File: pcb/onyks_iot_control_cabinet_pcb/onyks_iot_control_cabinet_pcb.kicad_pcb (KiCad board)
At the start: 2 copper layers, 80 x 90 mm, 37 parts, among them J1 Conn_01x02_Socket, J10 Conn_02x05_Odd_Even, J2 Conn_01x06_Socket, J3 Screw_Terminal_01x02, J4 Jack-DC, J6 Conn_02x09_Odd_Even, J7 Screw_Terminal_01x02, J8 Conn_01x06_Pin, J9 Conn_01x02_Socket, Q1 SQ4050EY-T1_GE3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

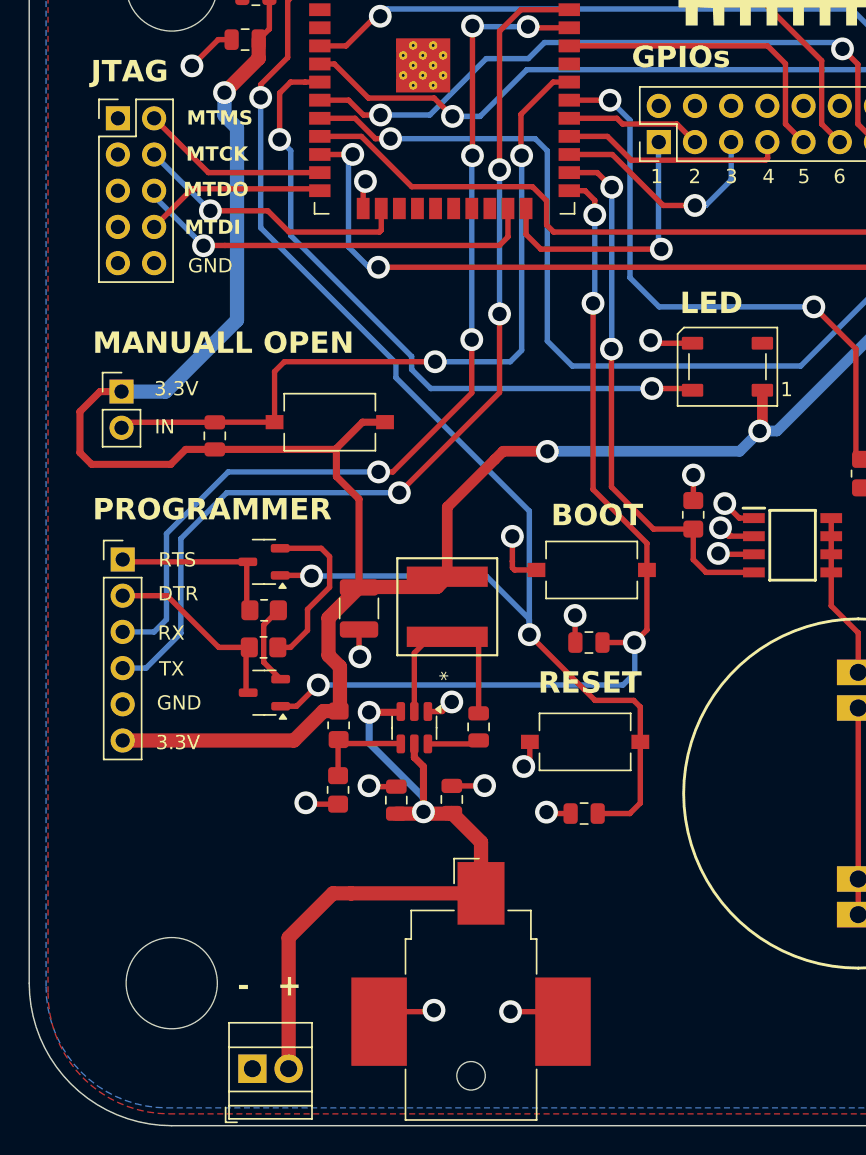
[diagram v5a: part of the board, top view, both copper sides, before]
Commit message: Add pins for the jumper and choosing the power supply; also add connection for JTAG 3V3
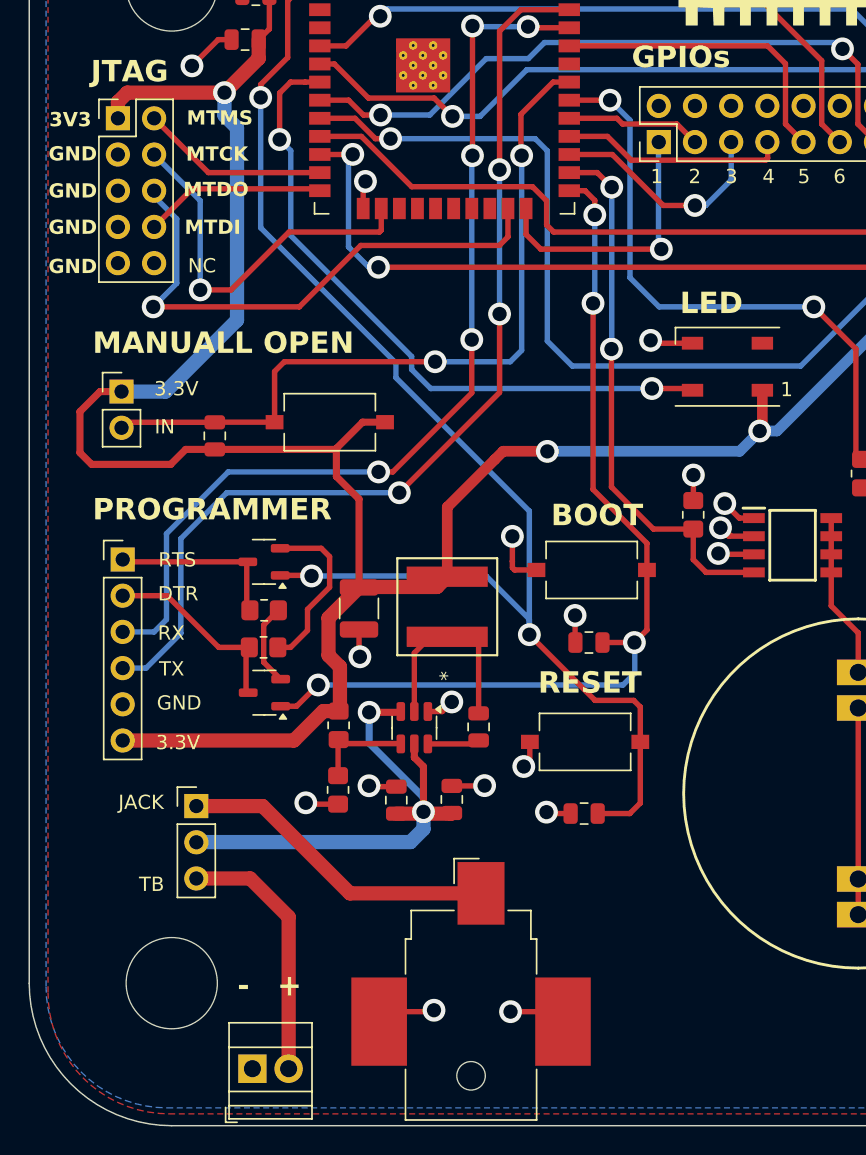
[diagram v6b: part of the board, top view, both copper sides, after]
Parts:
- added J5: Conn_01x03_Pin, Connector_PinHeader_2.54mm:PinHeader_1x03_P2.54mm_Vertical, F.Cu at (57.7, 93.6)
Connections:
- J10 pad 1: unconnected-(J10-Pin_1-Pad1) -> +3.3V
- J3 pad 2: V_IN -> Net-(J3-Pin_2)
- J4 pad 1: V_IN -> Net-(J5-Pin_1)
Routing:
- net Net-(J5-Pin_1): track 0.00 -> 22.5 mm
- net Net-(J3-Pin_2): track 0.00 -> 18.2 mm
- net V_IN: track 50.4 -> 37.4 mm
- net JTAG_MTDO: track 28.9 -> 38.4 mm
- net +3.3V: track 169.9 -> 178.8 mm
- net JTAG_MTCK: track 19.8 -> 26.8 mm
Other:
- board text added: "3V3"
- board text added: "JACK"
- board text added: "NC"
- board text added: "TB"

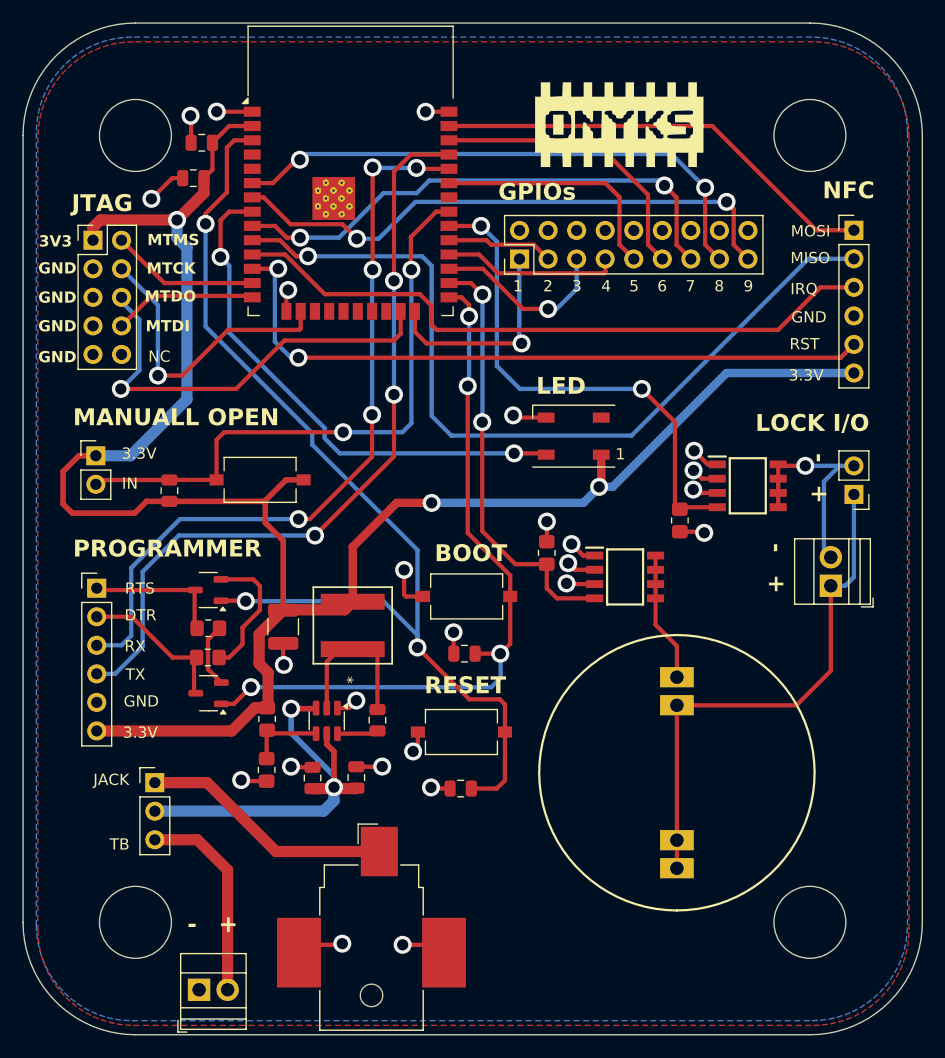
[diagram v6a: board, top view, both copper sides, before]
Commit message: Adding Thermal Relieves, Via stiching, Components Silkscreen
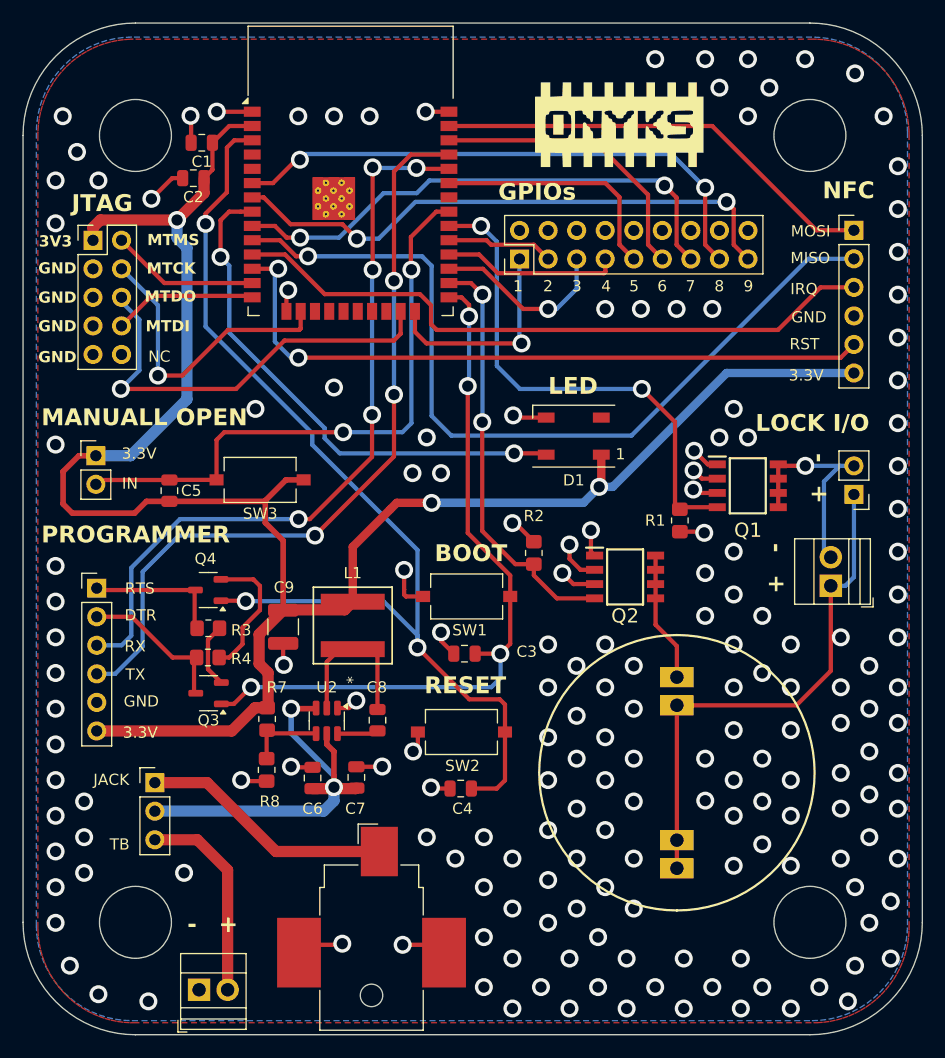
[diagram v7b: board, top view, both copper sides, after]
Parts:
- moved R2 1.15 mm to (91.4, 73.1)
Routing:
- net GND: track 64.1 -> 66.9 mm, vias 25 -> 180
- net BUZZER_SWITCH: track 38.2 -> 37.5 mm
- net LOCK_PLUS: vias 0 -> 1

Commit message: Onyks - Karol narzekal <3
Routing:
- net LOCK_PLUS: vias 1 -> 0
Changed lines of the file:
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@@
-		(net 29)
-	)
-	(via
-		(at 118.745 80.645)
-		(size 1.6)
-		(drill 1)
-		(layers "F.Cu" "B.Cu")
 		(net 29)
 	)
